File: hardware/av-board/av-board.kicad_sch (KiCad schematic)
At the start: 217 parts, among them J1 RCA Y, J10 2x20 socket, J2 RCA Pb, J3 RCA Pr, J4 RCA L, J5 RCA R, J6 HDMI-001, J9 2x20 socket, U1 ADV7842KBCZ-5, U2 ADV7511KSTZ, U3 PCM1808PWR, U4 TLV62569DBVR, U5 TPS7A7001DDAR, U6 TPS7A7001DDAR, U7 TPS7A7001DDAR, U8 TPD4E05U06DQAR, Y1 28.63636MHz 20pF

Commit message: av-board: 6 layers, placement for straight video buses, Freerouting 1.9.0
- 6-layer stack (signal/GND/signal/rail planes+signal/GND/signal): on 4
  layers Freerouting left ~100 connections around the BGA and diverged.
- ADV7842 at J10's height, its 75 R arrays in a column beside the pixel
  balls (regrouped by ball row), so the input bus runs straight into J10;
  ADV7511 level with J9. Rail planes exit away from the bus; filters
  fitted so their output pad lands in their plane.
- Standoffs on two diagonal Console holes; the other two blocked the
  buses. Console S1/S2 covered: two buttons of our own on J10 31/32.
- Vias for every ground/rail pad before routing; edge/window keepouts;
  power class 0.25 mm (0.5 mm-pitch supply pins); hole clearance 0.2.
- Freerouting 1.9.0 under a private Xvfb (2.5.0 diverges on this board).

Co-Authored-By: Claude Opus 5.5 <noreply@anthropic.com>
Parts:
- removed D1, D2, D3, D4, D5, D6, D7, D8: EZAEG2A50AX, lcsc:D0402, symbol lcsc:EZAEG2A50AX
- added R50: 2k, Resistor_SMD:R_0402_1005Metric, symbol Device:R
- added R51: 100k, Resistor_SMD:R_0402_1005Metric, symbol Device:R
- added SW1, SW2: TS-1187A-B-A-B, lcsc:SW-SMD_4P-L5.1-W5.1-P3.70-LS6.5-TL_H1.5, symbol lcsc:TS-1187A-B-A-B
- added U10, U9: TPD4E05U06DQAR, lcsc:USON-10_L2.5-W1.0-P0.50-BL, symbol lcsc:TPD4E05U06DQAR_C138714
- R1: value 169k -> 10k; LCSC C25758 -> C25744
- R10: value 24 -> 78.7k; LCSC C2909340 -> C67239
- R11: value 51 -> 30.1k; LCSC C25125 -> C29402
- R16: value 390k -> 24; LCSC C2909352 -> C2909340
- R17: value 499 -> 51; LCSC C4125 -> C25125
- R18: value 4.7k -> 390k; LCSC C25900 -> C2909352
- R19: value 4.7k -> 499; LCSC C25900 -> C4125
- R2: value 30.1k -> 10k; LCSC C29402 -> C25744
- R20: Note held in reset until the FPGA drives it -> (none)
- R22: Note (none) -> held in reset until the FPGA drives it
- R23: Note UG-214: TEST8 to 3.3 V via 4.7 k -> (none)
- R24: Note data sheet Rev B: TEST8 to GND via 4.7 k -> (none); now fitted
- R25: value 10k -> 4.7k; LCSC C25744 -> C25900; Note (none) -> UG-214: TEST8 to 3.3 V via 4.7 k
- R26: value 10k -> 4.7k; LCSC C25744 -> C25900; Note (none) -> data sheet Rev B: TEST8 to GND via 4.7 k; now not fitted
- R29, R30: value 4.7k -> 10k; LCSC C25900 -> C25744
- R3: value 316k -> 169k; LCSC C25777 -> C25758
- R31, R32: value 10k -> 4.7k; LCSC C25744 -> C25900
- R38, R39: value 51 -> 10k; LCSC C25125 -> C25744
- R4: value 100k -> 30.1k; LCSC C25741 -> C29402
- R42: value 887 -> 51; LCSC C55968414 -> C25125
- R43: value 2k -> 51; LCSC C4109 -> C25125
- R44: value 2k -> 887; LCSC C4109 -> C55968414
- R49: value 100k -> 2k; LCSC C25741 -> C4109; Note keeps HPD low with no cable (not in HWG Fig. 27) -> (none)
- R5: value 100k -> 316k; LCSC C25741 -> C25777
- R6: value 78.7k -> 100k; LCSC C67239 -> C25741
- R7: value 30.1k -> 100k; LCSC C29402 -> C25741
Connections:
- net 1V8A: now also R8.1; no longer R6.1
- net 1V8B: now also R10.1; no longer R8.1
- net 2V5: now also R5.1; no longer R3.1
- net 3V3: now also R2.1, R20.1, R24.1, R25.1, R3.1, R46.1, R47.1, R7.1; no longer R18.1, R19.1, R22.1, R43.1, R44.1, R5.1
- net AUD_DIV_L: now also R36.2, R37.1; no longer R34.2, R35.1
- net AUD_DIV_R: now also R38.2, R39.1; no longer R36.2, R37.1
- net AV_C0: now also RN1.1; no longer RN3.1
- net AV_C1: now also RN1.2; no longer RN3.2
- net AV_C2: now also RN1.3; no longer RN3.3
- net AV_C3: now also RN1.4; no longer RN3.4
- net AV_C4: now also RN2.3; no longer RN4.1
- net AV_C5: now also RN2.4; no longer RN4.2
- net AV_C6: now also RN3.2; no longer RN4.3
- net AV_C7: now also RN3.3; no longer RN4.4
- net AV_DE: now also RN3.1; no longer RN5.4
- net AV_HS: now also RN2.2; no longer RN5.2
- net AV_LLC: now also RN5.4; no longer RN5.1
- net AV_VS: now also RN2.1; no longer RN5.3
- net AV_Y0: now also RN3.4; no longer RN1.1
- net AV_Y1: now also RN4.1; no longer RN1.2
- net AV_Y2: now also RN4.2; no longer RN1.3
- net AV_Y3: now also RN4.3; no longer RN1.4
- net AV_Y4: now also RN4.4; no longer RN2.1
- net AV_Y5: now also RN5.1; no longer RN2.2
- net AV_Y6: now also RN5.2; no longer RN2.3
- net AV_Y7: now also RN5.3; no longer RN2.4
- net EN_1V8: now also R7.2; no longer R5.2
- net FB_1V8A: now also R8.2, R9.1; no longer R6.2, R7.1
- net FB_1V8B: now also R10.2, R11.1; no longer R8.2, R9.1
- net FB_2V5: now also R5.2, R6.1; no longer R3.2, R4.1
- net FB_3V3: now also R3.2, R4.1; no longer R1.2, R2.1
- net FMT: now also R35.1; no longer R33.1
- net GND: now also R19.2, R22.2, R34.2, R39.2, R44.2, R48.2, R6.2, R51.2, SW1.4 (D), SW2.4 (D), U10.3 (GND), U10.8 (GND), U9.3 (GND), U9.8 (GND); no longer J10.31, J10.32, R2.2, R20.2, R24.2, R25.2, R42.2, R46.2, R49.2, R7.2
- net HDMI_5V: now also R49.1, U8.6 (NC), R50.1; no longer R47.1, R48.1
- net HDMI_HPD: now also U8.7 (NC), R51.1; no longer R49.1
- net HDMI_SCL: now also R49.2, U8.10 (NC); no longer R47.2
- net HDMI_SDA: now also U8.9 (NC), R50.2; no longer R48.2
- net IN_C0: now also RN1.8; no longer RN3.8
- net IN_C1: now also RN1.7; no longer RN3.7
- net IN_C2: now also RN1.6; no longer RN3.6
- net IN_C3: now also RN1.5; no longer RN3.5
- net IN_C4: now also RN2.6; no longer RN4.8
- net IN_C5: now also RN2.5; no longer RN4.7
- net IN_C6: now also RN3.7; no longer RN4.6
- net IN_C7: now also RN3.6; no longer RN4.5
- net IN_DE: now also RN3.8; no longer RN5.5
- net IN_HS: now also RN2.7; no longer RN5.7
- net IN_INT1: now also R23.2; no longer R21.2
- net IN_LLC: now also RN5.5; no longer RN5.8
- net IN_RESET_N: now also R22.1; no longer R20.1
- net IN_SCL: now also R20.2; no longer R18.2
- net IN_SDA: now also R21.2; no longer R19.2
- net IN_VS: now also RN2.8; no longer RN5.6
- net IN_Y0: now also RN3.5; no longer RN1.8
- net IN_Y1: now also RN4.8; no longer RN1.7
- net IN_Y2: now also RN4.7; no longer RN1.6
- net IN_Y3: now also RN4.6; no longer RN1.5
- net IN_Y4: now also RN4.5; no longer RN2.8
- net IN_Y5: now also RN5.8; no longer RN2.7
- net IN_Y6: now also RN5.7; no longer RN2.6
- net IN_Y7: now also RN5.6; no longer RN2.5
- net MD0: now also R33.1; no longer R31.1
- net MD1: now also R34.1; no longer R32.1
- net OUT_I2S0: now also R43.1; no longer R41.1
- net OUT_INT: now also R47.2; no longer R45.2
- net OUT_LRCLK: now also R42.1; no longer R40.1
- net OUT_MCLK: now also R40.1; no longer R38.1
- net OUT_PD: now also R48.1; no longer R46.1
- net OUT_SCL: now also R45.2; no longer R43.2
- net OUT_SCLK: now also R41.1; no longer R39.1
- net OUT_SDA: now also R46.2; no longer R44.2
- net PD_DDCA_SCL: now also R28.1; no longer R26.1
- net PD_DDCB_SCL: now also R27.1; no longer R25.1
- net PD_SDRAM_LDQS: now also R31.1; no longer R29.1
- net PD_SDRAM_UDQS: now also R32.1; no longer R30.1
- net PD_TTX_SCL: now also R30.1; no longer R28.1
- net PD_VGA_SCL: now also R29.1; no longer R27.1
- net PWRDN1: now also R24.2; no longer R22.2
- net RCA_L: now also R36.1; no longer R34.1
- net RCA_PB: now also R14.1; no longer R12.1
- net RCA_PR: now also R16.1; no longer R14.1
- net RCA_R: now also R38.1; no longer R36.1
- net RCA_Y: now also R12.1; no longer R10.1
- net RTERM: now also R19.1; no longer R17.1
- net R_EXT: now also R44.1; no longer R42.1
- net TERM_PB: now also R14.2, R15.1; no longer R12.2, R13.1
- net TERM_PR: now also R16.2, R17.1; no longer R14.2, R15.1
- net TERM_Y: now also R12.2, R13.1; no longer R10.2, R11.1
- net TEST8: now also R25.2, R26.1; no longer R23.2, R24.1
- net TMDS_CKN: now also U10.5 (D2-), U10.6 (NC)
- net TMDS_CKP: now also U10.4 (D2+), U10.7 (NC)
- net TMDS_D0N: now also U10.2 (D1-), U10.9 (NC)
- net TMDS_D0P: now also U10.1 (D1+), U10.10 (NC)
- net TMDS_D1N: now also U9.5 (D2-), U9.6 (NC)
- net TMDS_D1P: now also U9.4 (D2+), U9.7 (NC)
- net TMDS_D2N: now also U9.2 (D1-), U9.9 (NC)
- net TMDS_D2P: now also U9.1 (D1+), U9.10 (NC)
- net TX_I2S0: now also R43.2; no longer R41.2
- net TX_LRCLK: now also R42.2; no longer R40.2
- net TX_MCLK: now also R40.2; no longer R38.2
- net TX_SCLK: now also R41.2; no longer R39.2
- net XTALN: now also R18.2; no longer R16.2
- net XTALP: now also R18.1; no longer R16.1
- new net IN_KEY1: J10.31, R1.2, SW1.1 (A)
- new net IN_KEY2: J10.32, R2.2, SW2.1 (A)
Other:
- moved on the sheet: C111, C112, C113, C114, C115, C116, C117, C118, C119, C120, C121, C122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

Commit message: av-board: routing fixes (locked/restored fanout, plane keepouts, PVDD plane, corridors)
- Fanout copper locked and put back after the session import (KiCad
  replaces all copper with Freerouting's result).
- In3 rail planes: no signal tracks across them (In3-only keepouts); inner
  plane clearance 0.127 mm, so the planes survive the BGA's via field.
- PVDD gets its own small plane and its filter beside it.
- SDRAM DQ pull-downs as single 0402s beside their balls (UG-214 App. C).
- Bus corridors kept free of small parts; stitching vias; two-stage route.

Co-Authored-By: Claude Opus 5.5 <noreply@anthropic.com>
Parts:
- removed RN6, RN7, RN8, RN9: 4.7k, lcsc:RES-ARRAY-SMD_0402-8P-L2.0-W1.0-BL, symbol lcsc:4D02WGJ0472TCE
- added R52, R53, R54, R55: 10k, Resistor_SMD:R_0402_1005Metric, symbol Device:R
- added R56, R57, R58, R59: 51, Resistor_SMD:R_0402_1005Metric, symbol Device:R
- added R60: 887, Resistor_SMD:R_0402_1005Metric, symbol Device:R
- added R61, R62, R63, R64, R65, R66: 2k, Resistor_SMD:R_0402_1005Metric, symbol Device:R
- added R67: 100k, Resistor_SMD:R_0402_1005Metric, symbol Device:R
- R33, R34, R35, R36, R37, R38, R39: value 10k -> 4.7k; LCSC C25744 -> C25900
- R40, R41, R42, R43: value 51 -> 4.7k; LCSC C25125 -> C25900
- R44: value 887 -> 4.7k; LCSC C55968414 -> C25900
- R45, R46, R47, R48: value 2k -> 4.7k; LCSC C4109 -> C25900
- R49, R50: value 2k -> 10k; LCSC C4109 -> C25744
- R51: value 100k -> 10k; LCSC C25741 -> C25744; Note keeps HPD low with no cable (not in HWG Fig. 27) -> (none)
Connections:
- net 3V3: now also R61.1, R62.1, R63.1; no longer R45.1, R46.1, R47.1
- net AUD_DIV_L: now also R52.2, R53.1; no longer R36.2, R37.1
- net AUD_DIV_R: now also R54.2, R55.1; no longer R38.2, R39.1
- net FMT: now also R51.1; no longer R35.1
- net GND: now also R36.2, R38.2, R40.2, R41.2, R42.2, R43.2, R45.2, R46.2, R47.2, R49.2, R50.2, R53.2, R55.2, R60.2, R64.2, R67.2
- net HDMI_5V: now also R65.1, R66.1; no longer R49.1, R50.1
- net HDMI_HPD: now also R67.1; no longer R51.1
- net HDMI_SCL: now also R65.2; no longer R49.2
- net HDMI_SDA: now also R66.2; no longer R50.2
- net MD0: now also R49.1; no longer R33.1
- net MD1: now also R50.1; no longer R34.1
- net OUT_I2S0: now also R59.1; no longer R43.1
- net OUT_INT: now also R63.2; no longer R47.2
- net OUT_LRCLK: now also R58.1; no longer R42.1
- net OUT_MCLK: now also R56.1; no longer R40.1
- net OUT_PD: now also R64.1; no longer R48.1
- net OUT_SCL: now also R61.2; no longer R45.2
- net OUT_SCLK: now also R57.1; no longer R41.1
- net OUT_SDA: now also R62.2; no longer R46.2
- net PD_SDRAM_DQ0: now also R31.1
- net PD_SDRAM_DQ1: now also R32.1
- net PD_SDRAM_DQ10: now also R41.1
- net PD_SDRAM_DQ11: now also R42.1
- net PD_SDRAM_DQ12: now also R43.1
- net PD_SDRAM_DQ13: now also R44.1
- net PD_SDRAM_DQ14: now also R45.1
- net PD_SDRAM_DQ15: now also R46.1
- net PD_SDRAM_DQ2: now also R33.1
- net PD_SDRAM_DQ3: now also R34.1
- net PD_SDRAM_DQ4: now also R35.1
- net PD_SDRAM_DQ5: now also R36.1
- net PD_SDRAM_DQ6: now also R37.1
- net PD_SDRAM_DQ7: now also R38.1
- net PD_SDRAM_DQ8: now also R39.1
- net PD_SDRAM_DQ9: now also R40.1
- net PD_SDRAM_LDQS: now also R47.1; no longer R31.1
- net PD_SDRAM_UDQS: now also R48.1; no longer R32.1
- net RCA_L: now also R52.1; no longer R36.1
- net RCA_R: now also R54.1; no longer R38.1
- net R_EXT: now also R60.1; no longer R44.1
- net TX_I2S0: now also R59.2; no longer R43.2
- net TX_LRCLK: now also R58.2; no longer R42.2
- net TX_MCLK: now also R56.2; no longer R40.2
- net TX_SCLK: now also R57.2; no longer R41.2
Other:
- moved on the sheet: C100, C38, C39, C40, C41, C42, C43, C44, C45, C46, C47, C48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

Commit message: av-board: drop the window-era workarounds
Back to Freerouting 2.5 (headless; no 1.9.0/Xvfb, no second stage), 4
layers by default (LAYERS=6 still available), no reserved bus
corridors, SDRAM DQ pull-downs as 4.7 k arrays again. Kept: the
no-window placement, plane design and fanout, locked/restored fanout,
plane keepouts, rules, placer anchoring.

Co-Authored-By: Claude Opus 5.5 <noreply@anthropic.com>
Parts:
- removed R52, R53, R54, R55: 10k, Resistor_SMD:R_0402_1005Metric, symbol Device:R
- removed R56, R57, R58, R59: 51, Resistor_SMD:R_0402_1005Metric, symbol Device:R
- removed R60: 887, Resistor_SMD:R_0402_1005Metric, symbol Device:R
- removed R61, R62, R63, R64, R65, R66: 2k, Resistor_SMD:R_0402_1005Metric, symbol Device:R
- removed R67: 100k, Resistor_SMD:R_0402_1005Metric, symbol Device:R
- added RN6, RN7, RN8, RN9: 4.7k, lcsc:RES-ARRAY-SMD_0402-8P-L2.0-W1.0-BL, symbol lcsc:4D02WGJ0472TCE
- R33, R34, R35, R36, R37, R38, R39: value 4.7k -> 10k; LCSC C25900 -> C25744
- R40, R41, R42, R43: value 4.7k -> 51; LCSC C25900 -> C25125
- R44: value 4.7k -> 887; LCSC C25900 -> C55968414
- R45, R46, R47, R48: value 4.7k -> 2k; LCSC C25900 -> C4109
- R49, R50: value 10k -> 2k; LCSC C25744 -> C4109
- R51: value 10k -> 100k; LCSC C25744 -> C25741; Note (none) -> keeps HPD low with no cable (not in HWG Fig. 27)
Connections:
- net 3V3: now also R45.1, R46.1, R47.1
- net AUD_DIV_L: now also R36.2, R37.1
- net AUD_DIV_R: now also R38.2, R39.1
- net FMT: now also R35.1; no longer R51.1
- net GND: now also RN6.5, RN6.6, RN6.7, RN6.8, RN7.5, RN7.6, RN7.7, RN7.8, RN8.5, RN8.6, RN8.7, RN8.8, RN9.5, RN9.6, RN9.7, RN9.8; no longer R36.2, R38.2, R40.2, R41.2, R42.2, R43.2, R45.2, R46.2, R47.2, R49.2, R50.2
- net HDMI_5V: now also R49.1, R50.1
- net HDMI_HPD: now also R51.1
- net HDMI_SCL: now also R49.2
- net HDMI_SDA: now also R50.2
- net MD0: now also R33.1; no longer R49.1
- net MD1: now also R34.1; no longer R50.1
- net OUT_I2S0: now also R43.1
- net OUT_INT: now also R47.2
- net OUT_LRCLK: now also R42.1
- net OUT_MCLK: now also R40.1
- net OUT_PD: now also R48.1
- net OUT_SCL: now also R45.2
- net OUT_SCLK: now also R41.1
- net OUT_SDA: now also R46.2
- net PD_SDRAM_DQ0: now also RN6.1; no longer R31.1
- net PD_SDRAM_DQ1: now also RN6.2; no longer R32.1
- net PD_SDRAM_DQ10: now also RN8.3; no longer R41.1
- net PD_SDRAM_DQ11: now also RN8.4; no longer R42.1
- net PD_SDRAM_DQ12: now also RN9.1; no longer R43.1
- net PD_SDRAM_DQ13: now also RN9.2; no longer R44.1
- net PD_SDRAM_DQ14: now also RN9.3; no longer R45.1
- net PD_SDRAM_DQ15: now also RN9.4; no longer R46.1
- net PD_SDRAM_DQ2: now also RN6.3; no longer R33.1
- net PD_SDRAM_DQ3: now also RN6.4; no longer R34.1
- net PD_SDRAM_DQ4: now also RN7.1; no longer R35.1
- net PD_SDRAM_DQ5: now also RN7.2; no longer R36.1
- net PD_SDRAM_DQ6: now also RN7.3; no longer R37.1
- net PD_SDRAM_DQ7: now also RN7.4; no longer R38.1
- net PD_SDRAM_DQ8: now also RN8.1; no longer R39.1
- net PD_SDRAM_DQ9: now also RN8.2; no longer R40.1
- net PD_SDRAM_LDQS: now also R31.1; no longer R47.1
- net PD_SDRAM_UDQS: now also R32.1; no longer R48.1
- net RCA_L: now also R36.1
- net RCA_R: now also R38.1
- net R_EXT: now also R44.1
- net TX_I2S0: now also R43.2
- net TX_LRCLK: now also R42.2
- net TX_MCLK: now also R40.2
- net TX_SCLK: now also R41.2
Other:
- moved on the sheet: C100, C38, C39, C40, C41, C42, C43, C44, C45, C46, C47, C48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

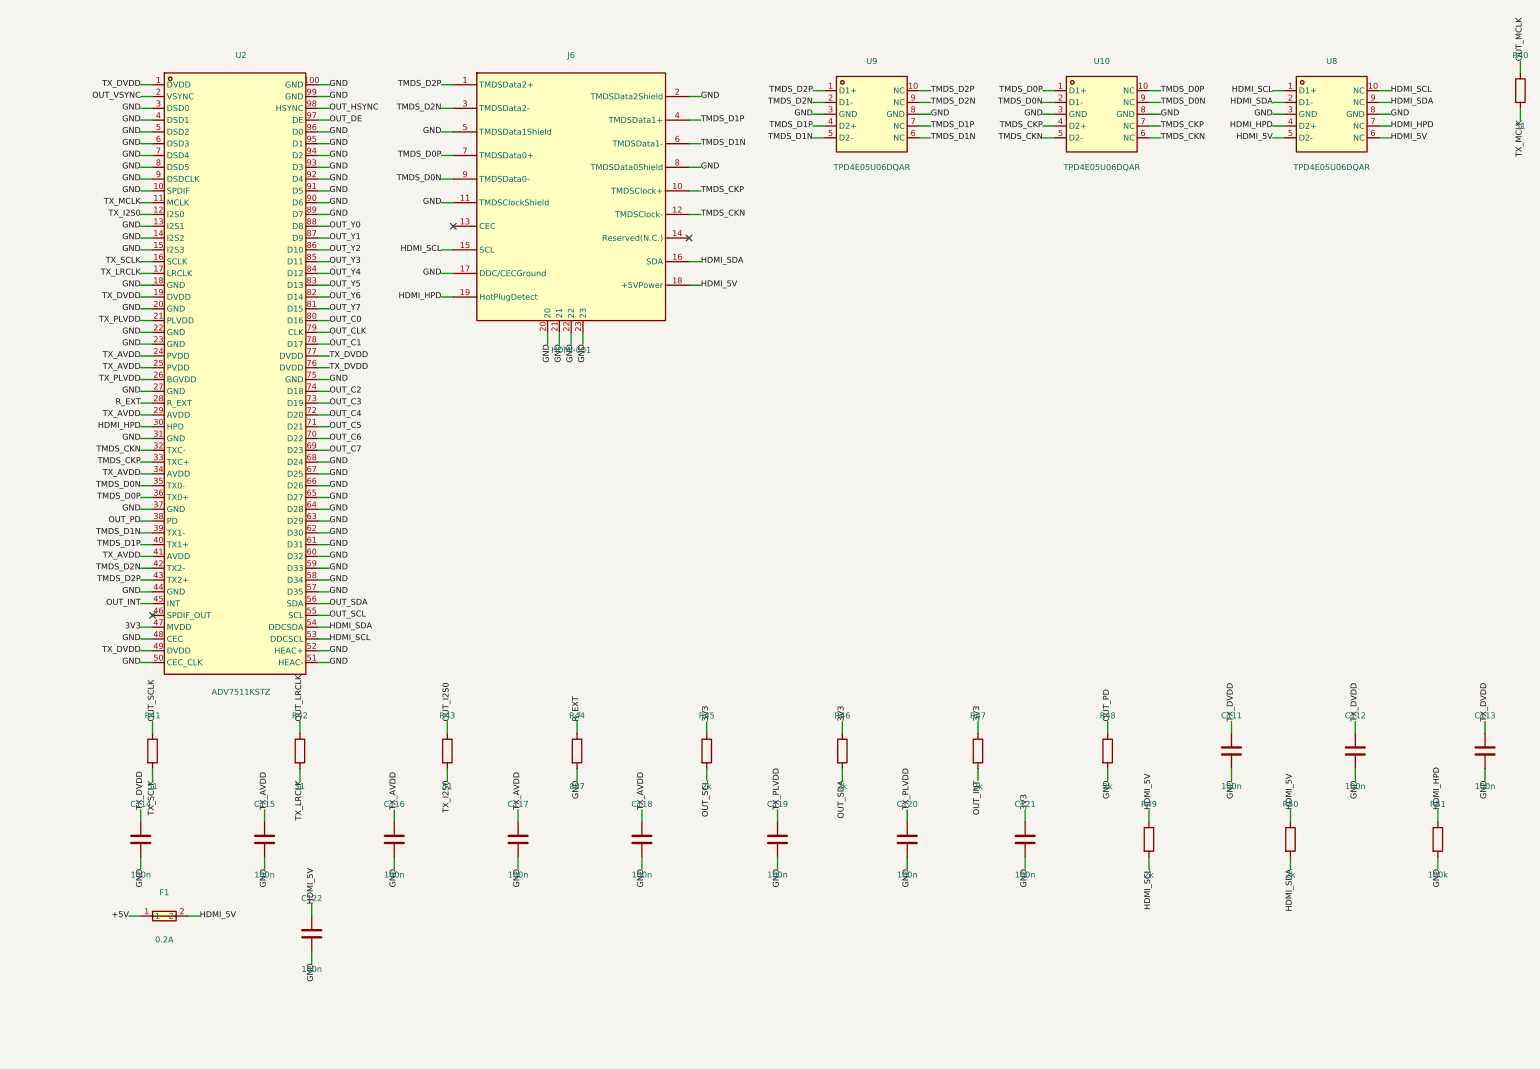
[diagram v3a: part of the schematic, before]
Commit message: av-board: DeepPCB client, TMDS nets as _P/_N pairs, Freerouting selectable
- deeppcb.py: route a DSN on DeepPCB through its public API (key from
  ~/.config/deeppcb/key, never the repo): upload, resubmit as DeepPCB
  JSON with the board-edge clearance and the TMDS differential pairs
  (a DSN carries neither), route keeping our wiring, poll, fetch the
  session. gen_pcb.py imports any session with SES=file.
- TMDS nets renamed TMDS_X_P/_N so KiCad and DeepPCB see pairs; TMDS
  class pair geometry 0.25/0.2 mm (~97 R, to check with JLCPCB).
- Rail planes reach their caps and filters; FREEROUTING selects the
  Freerouting version (1.9.0 by default, via a private Xvfb).

Co-Authored-By: Claude Opus 5.5 <noreply@anthropic.com>
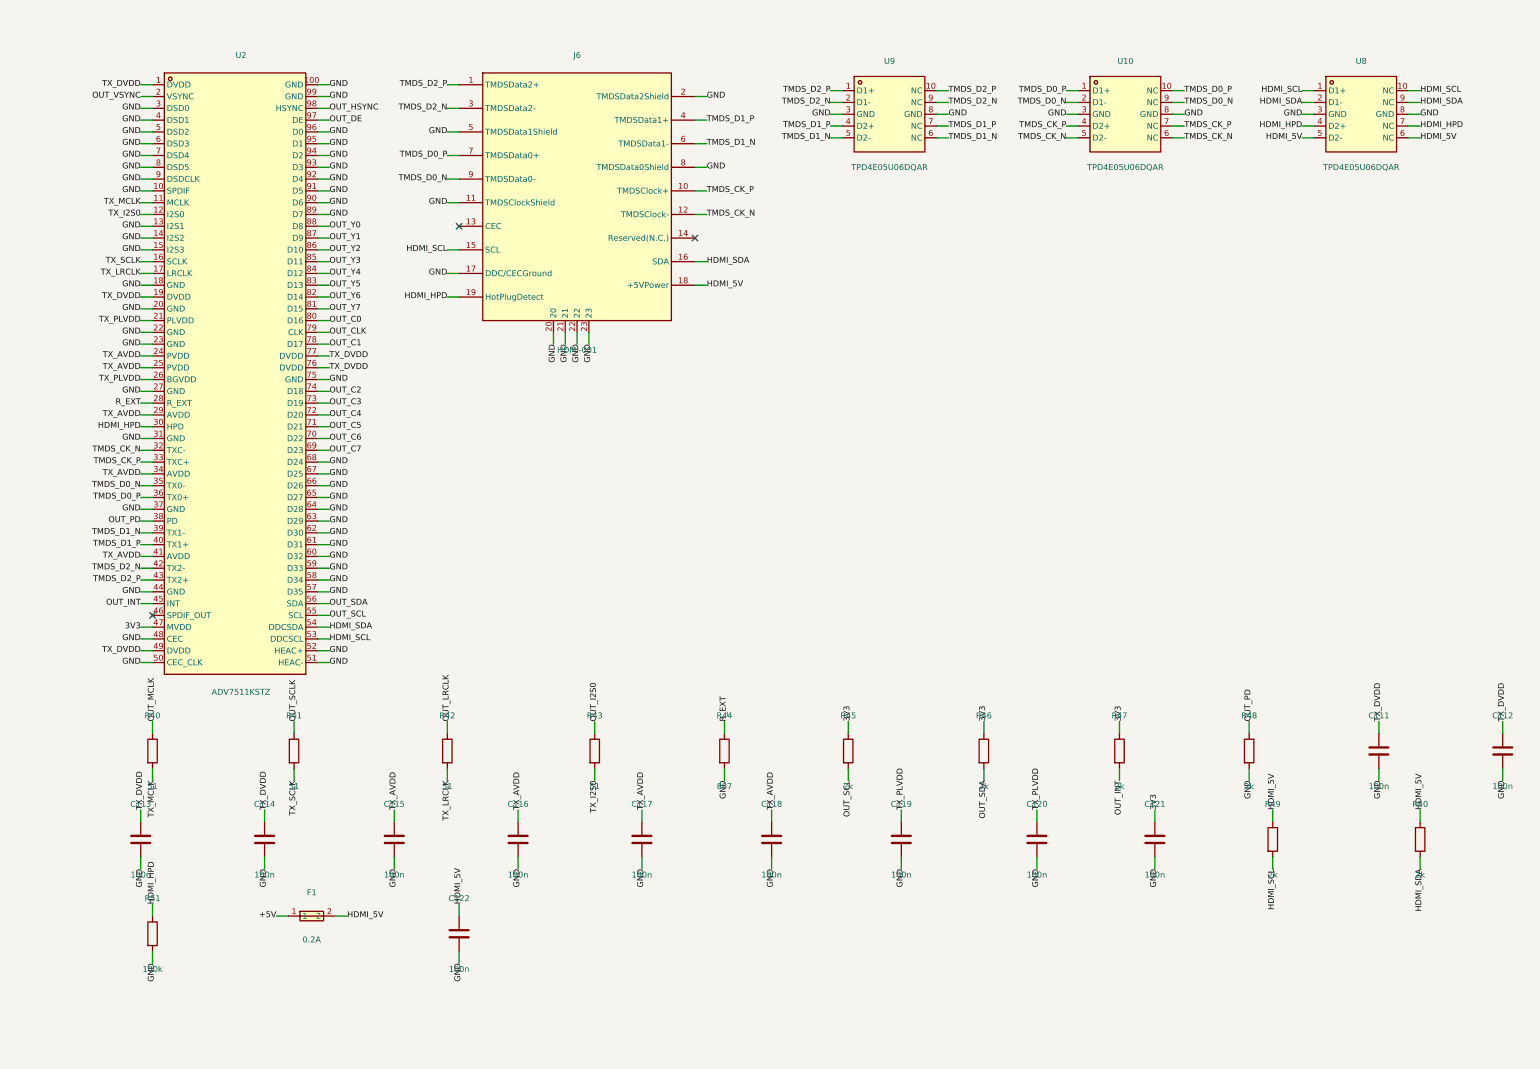
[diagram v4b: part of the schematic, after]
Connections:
- net TMDS_CKN renamed TMDS_CK_N
- net TMDS_CKP renamed TMDS_CK_P
- net TMDS_D0N renamed TMDS_D0_N
- net TMDS_D0P renamed TMDS_D0_P
- net TMDS_D1N renamed TMDS_D1_N
- net TMDS_D1P renamed TMDS_D1_P
- net TMDS_D2N renamed TMDS_D2_N
- net TMDS_D2P renamed TMDS_D2_P
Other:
- moved on the sheet: C111, C112, C113, C114, C115, C116, C117, C118, C119, C120, C121, C122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
